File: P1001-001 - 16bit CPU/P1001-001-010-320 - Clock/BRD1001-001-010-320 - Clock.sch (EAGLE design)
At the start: 15 parts, among them IC1 74HC192D, IC12 74AC245DW, IC2 74HC192D, IC27 MEGA8535-A, IC3 74HC192D, IC4 74HC192D, IC7 74AC245DW, J1 22-27-2041-04

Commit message: Finish ALI Counter
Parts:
- removed BOTTOMBUS, FRONTBUS: (no value), con-harting-ml:ML16
- removed IC1, IC2: 74HC192D, 74xx-eu:74HC192D
- removed IC12, IC7: 74AC245DW, 74xx-eu:74AC245DW
- removed IC27: MEGA8535-A, atmel:MEGA8535-A
- removed J1: 22-27-2041-04, con-molex:22-27-2041-04
- removed JP2: (no value), jumper:JP4E
- removed RN2: (no value), resistor-dil:10R-NSOMC
- removed SV5: (no value), con-harting-ml:ML6
- added !CLOCKPIN, VCC_GND1, VCC_GND2: (no value), con-harting-ml:ML16
- added C1, C5, C6: .01uF, rcl:C-USC1206
- added C2: 1uF, rcl:C-USC1206
- added C7: .1uF, rcl:C-USC1206
- added CN1: (no value), adafruit:DCBARRELPTH
- added IC5: 74LS32D, 74xx-us:74LS32D
- added JP1: (no value), jumper:JP2E
- added LED1: (no value), led:LED5MM
- added R1, R2, R4, R5, R7: 1k, rcl:R-US_M1206
- added R3: 1M, rcl:R-US_M1206
- added R6: (no value), rcl:R-US_M1206
- added S1: (no value), switch-omron:40-XX
- added U$10, U$11, U$12, U$5, U$6, U$7, U$8, U$9: AZ1117E, 16bit:AZ1117E
- added U$2, U$3, U$4: NA555, 16bit:NA555
- IC3: value 74HC192D -> 74ALS04D; device 74xx-eu:74HC192D -> 74xx-us:74ALS04D
- IC4: value 74HC192D -> 74ALS08D; device 74xx-eu:74HC192D -> 74xx-us:74ALS08D
- U$1: value 4-DIGIT-7-SEGMENT -> 3310H-001-105L; device ADAFRUIT:4-DIGIT-7-SEGMENT -> 16bit:3310H-001-105L
- renumbered BACKBUS to CLOCKPIN
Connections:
- removed net !DEC: IC1A.DN, JP2.3
- removed net !INC: IC1A.UP, JP2.2
- removed net !REG_IN: IC1A.LD, IC2A.LD, IC3A.LD, IC4A.LD, JP2.1
- removed net !REG_OUT: IC12A.G, IC7A.G, JP2.4
- removed net A: IC27.(ADC0)PA0, RN2A.2
- removed net B: IC27.(ADC1)PA1, RN2B.2
- removed net BUS0: CLOCKPIN.1, FRONTBUS.1, IC12A.A8, IC1A.D
- removed net BUS1: CLOCKPIN.2, FRONTBUS.2, IC12A.A7, IC1A.C
- removed net BUS10: CLOCKPIN.11, FRONTBUS.11, IC3A.B, IC7A.A6
- removed net BUS11: CLOCKPIN.12, FRONTBUS.12, IC3A.A, IC7A.A5
- removed net BUS12: CLOCKPIN.13, FRONTBUS.13, IC4A.D, IC7A.A4
- removed net BUS13: CLOCKPIN.14, FRONTBUS.14, IC4A.C, IC7A.A3
- removed net BUS14: CLOCKPIN.15, FRONTBUS.15, IC4A.B, IC7A.A2
- removed net BUS15: CLOCKPIN.16, FRONTBUS.16, IC4A.A, IC7A.A1
- removed net BUS2: CLOCKPIN.3, FRONTBUS.3, IC12A.A6, IC1A.B
- removed net BUS3: CLOCKPIN.4, FRONTBUS.4, IC12A.A5, IC1A.A
- removed net BUS4: CLOCKPIN.5, FRONTBUS.5, IC12A.A4, IC2A.D
- removed net BUS5: CLOCKPIN.6, FRONTBUS.6, IC12A.A3, IC2A.C
- removed net BUS6: CLOCKPIN.7, FRONTBUS.7, IC12A.A2, IC2A.B
- removed net BUS7: CLOCKPIN.8, FRONTBUS.8, IC12A.A1, IC2A.A
- removed net BUS8: CLOCKPIN.9, FRONTBUS.9, IC3A.D, IC7A.A8
- removed net BUS9: CLOCKPIN.10, FRONTBUS.10, IC3A.C, IC7A.A7
- removed net C: IC27.(ADC2)PA2, RN2C.2
- removed net CLEAR: IC1A.CLR, IC2A.CLR, IC3A.CLR, IC4A.CLR, J1-4.S
- removed net D: IC27.(ADC3)PA3, RN2D.2
- removed net DIG0: IC27.(T0/XCK)PB0, U$1.DIG1
- removed net DIG1: IC27.(T1)PB1, U$1.DIG2
- removed net DIG2: IC27.(AIN0/INT2)PB2, U$1.DIG3
- removed net DIG3: IC27.(AIN1/OC0)PB3, U$1.DIG4
- removed net DP: IC27.(ADC7)PA7, RN2H.2
- removed net E: IC27.(ADC4)PA4, RN2E.2
- removed net F: IC27.(ADC5)PA5, RN2F.2
- removed net G: IC27.(ADC6)PA6, RN2G.2
- removed net N$18: IC27.(MOSI)PB5, SV5.3
- removed net N$19: IC27.(SCK)PB7, SV5.4
- removed net N$20: IC27.(MISO)PB6, SV5.6
- removed net N$21: IC27.RESET, SV5.2
- removed net N$24: RN2A.1, U$1.A
- removed net N$25: RN2B.1, U$1.B
- removed net N$26: RN2C.1, U$1.C
- removed net N$27: RN2D.1, U$1.D
- removed net N$28: RN2E.1, U$1.E
- removed net N$29: RN2F.1, U$1.F
- removed net N$30: RN2G.1, U$1.G
- removed net N$31: RN2H.1, U$1.DP
- removed net N$7: IC3A.BO, IC4A.DN
- removed net SIGNAL0: BOTTOMBUS.1, IC12A.B8, IC1A.QD, IC27.(RXD)PD0
- removed net SIGNAL1: BOTTOMBUS.2, IC12A.B7, IC1A.QC, IC27.(TXD)PD1
- removed net SIGNAL10: BOTTOMBUS.11, IC27.PC2, IC3A.QB, IC7A.B6
- removed net SIGNAL11: BOTTOMBUS.12, IC27.PC3, IC3A.QA, IC7A.B5
- removed net SIGNAL12: BOTTOMBUS.13, IC27.PC4, IC4A.QD, IC7A.B4
- removed net SIGNAL13: BOTTOMBUS.14, IC27.PC5, IC4A.QC, IC7A.B3
- removed net SIGNAL14: BOTTOMBUS.15, IC27.(TOSC1)PC6, IC4A.QB, IC7A.B2
- removed net SIGNAL15: BOTTOMBUS.16, IC27.(TOSC2)PC7, IC4A.QA, IC7A.B1
- removed net SIGNAL2: BOTTOMBUS.3, IC12A.B6, IC1A.QB, IC27.(INT0)PD2
- removed net SIGNAL3: BOTTOMBUS.4, IC12A.B5, IC1A.QA, IC27.(INT1)PD3
- removed net SIGNAL4: BOTTOMBUS.5, IC12A.B4, IC27.(OC1B)PD4, IC2A.QD
- removed net SIGNAL5: BOTTOMBUS.6, IC12A.B3, IC27.(OC1A)PD5, IC2A.QC
- removed net SIGNAL6: BOTTOMBUS.7, IC12A.B2, IC27.(ICP)PD6, IC2A.QB
- removed net SIGNAL7: BOTTOMBUS.8, IC12A.B1, IC27.(OC2)PD7, IC2A.QA
- removed net SIGNAL8: BOTTOMBUS.9, IC27.PC0(SCL), IC3A.QD, IC7A.B8
- removed net SIGNAL9: BOTTOMBUS.10, IC27.PC1(SDA), IC3A.QC, IC7A.B7
- new net !CLK: !CLOCKPIN.1, !CLOCKPIN.10, !CLOCKPIN.11, !CLOCKPIN.12, !CLOCKPIN.13, !CLOCKPIN.14, !CLOCKPIN.15, !CLOCKPIN.16, !CLOCKPIN.2, !CLOCKPIN.3, !CLOCKPIN.4, !CLOCKPIN.5, !CLOCKPIN.6, !CLOCKPIN.7, !CLOCKPIN.8, !CLOCKPIN.9, IC3C.O
- new net !HALT: IC4C.I1
- new net IN: CN1.PWR, U$10.INPUT, U$11.INPUT, U$12.INPUT, U$5.INPUT, U$6.INPUT, U$7.INPUT, U$8.INPUT, U$9.INPUT
- new net N$10: C6.1, U$4.CONT
- new net N$11: C5.1, U$3.CONT
- new net N$12: IC3A.I, IC4A.I0, U$4.OUT
- new net N$13: IC4A.I1, JP1.3, R1.1, R2.1, U$2.OUT
- new net N$14: IC4B.I0, U$3.OUT
- new net N$15: IC3A.O, IC4B.I1
- new net N$16: IC4A.O, IC5A.I0
- new net N$17: IC4B.O, IC5A.I1
- new net N$22: IC4C.I0, IC5A.O
- new net N$8: C2.1, U$1.START1, U$2.THRES, U$2.TRIG
- new net N$9: C1.1, U$2.CONT
- new net VCC1: S1.S, S1.S1, U$3.TRIG
- net CLK: now also CLOCKPIN.1, CLOCKPIN.10, CLOCKPIN.11, CLOCKPIN.12, CLOCKPIN.13, CLOCKPIN.14, CLOCKPIN.15, CLOCKPIN.16, CLOCKPIN.2, CLOCKPIN.3, CLOCKPIN.4, CLOCKPIN.5, CLOCKPIN.6, CLOCKPIN.7, CLOCKPIN.8, CLOCKPIN.9, IC3C.I, IC4C.O, LED1.A; no longer J1-3.S
- net GND: now also C1.2, C2.2, C5.2, C6.2, C7.2, CN1.GND, JP1.2, R6.1, U$10.GND, U$11.GND, U$12.GND, U$2.GND, U$3.GND, U$4.GND, U$4.THRES, U$5.GND, U$6.GND, U$7.GND, U$8.GND, U$9.GND, VCC_GND1.1, VCC_GND1.11, VCC_GND1.13, VCC_GND1.15, VCC_GND1.3, VCC_GND1.5, VCC_GND1.7, VCC_GND1.9, VCC_GND2.1, VCC_GND2.11, VCC_GND2.13, VCC_GND2.15, VCC_GND2.3, VCC_GND2.5, VCC_GND2.7, VCC_GND2.9; no longer IC12A.DIR, IC27.AREF, IC27.GND, IC27.GND1, IC27.GND2, IC27.GND@1, IC7A.DIR, J1-1.S, SV5.1
- net N$1: now also R5.1, R7.1, U$2.DISCH; no longer IC4A.BO
- net N$2: now also R7.2, U$1.SCRUB1; no longer IC1A.CO, IC2A.UP
- net N$3: now also LED1.C, R6.2; no longer IC1A.BO, IC2A.DN
- net N$4: now also R2.2, U$4.TRIG; no longer IC2A.CO, IC3A.UP
- net N$5: now also R4.2, S1.P, S1.P1; no longer IC2A.BO, IC3A.DN
- net N$6: now also C7.1, R3.1, U$3.DISCH, U$3.THRES; no longer IC3A.CO, IC4A.UP
- net VCC: now also JP1.1, R1.2, R3.2, R4.1, R5.2, U$10.OUTPUT, U$11.OUTPUT, U$12.OUTPUT, U$2.RESET, U$2.VCC, U$3.RESET, U$3.VCC, U$4.RESET, U$4.VCC, U$5.OUTPUT, U$6.OUTPUT, U$7.OUTPUT, U$8.OUTPUT, U$9.OUTPUT, VCC_GND1.10, VCC_GND1.12, VCC_GND1.14, VCC_GND1.16, VCC_GND1.2, VCC_GND1.4, VCC_GND1.6, VCC_GND1.8, VCC_GND2.10, VCC_GND2.12, VCC_GND2.14, VCC_GND2.16, VCC_GND2.2, VCC_GND2.4, VCC_GND2.6, VCC_GND2.8; no longer IC27.AVCC, IC27.VCC, IC27.VCC1, IC27.VCC2, J1-2.S, SV5.5

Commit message: Check in the first try at soldering up the board
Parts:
- added AUTO, PULSE, SWITCH: NA555, 16bit:NA555
- added JP2: (no value), jumper:JP2E
- added U$13: AZ1117E, 16bit:AZ1117E
- U$2, U$3, U$4: value NA555 -> AZ1117E; device 16bit:NA555 -> 16bit:AZ1117E
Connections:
- removed net N$12: IC3A.I, IC4A.I0, U$4.OUT
- removed net N$5 (its old number): R4.2, S1.P, S1.P1
- removed net VCC1: S1.S, S1.S1, U$3.TRIG
- new net AUTOOUT: AUTO.OUT, IC4A.I0
- new net N$7: PULSE.TRIG, R4.1, S1.S, S1.S1
- new net PULSEOUT: IC4B.I0, PULSE.OUT
- new net SWITCHOUT: IC3A.I, IC4A.I1, SWITCH.OUT
- net !HALT: now also JP2.3
- net GND: now also AUTO.GND, PULSE.GND, S1.P, S1.P1, SWITCH.GND, SWITCH.THRES, U$13.GND; no longer C1.2, U$4.THRES
- net IN: now also U$13.INPUT, U$2.INPUT, U$3.INPUT, U$4.INPUT
- net N$1: now also AUTO.THRES, AUTO.TRIG, C2.1, U$1.START1; no longer R5.1, R7.1, U$2.DISCH
- net N$10: now also PULSE.DISCH, R3.1; no longer C6.1, U$4.CONT
- net N$11: now also C6.1, SWITCH.CONT; no longer C5.1, U$3.CONT
- net N$13: now also SWITCH.RESET; no longer IC4A.I1, R1.1, U$2.OUT
- net N$14: now also JP1.1, R1.1, SWITCH.TRIG; no longer IC4B.I0, U$3.OUT
- net N$4: now also AUTO.CONT, C1.1; no longer R2.2, U$4.TRIG
- net N$6: now also AUTO.DISCH, R5.1, R7.1; no longer C7.1, R3.1, U$3.DISCH, U$3.THRES
- net N$8: now also C7.1, PULSE.THRES; no longer C2.1, U$1.START1, U$2.THRES, U$2.TRIG
- net N$9: now also C5.1, PULSE.CONT; no longer C1.1, U$2.CONT
- net VCC: now also AUTO.RESET, AUTO.VCC, C1.2, PULSE.RESET, PULSE.VCC, R2.2, R4.2, SWITCH.VCC, U$13.OUTPUT, U$2.OUTPUT, U$3.OUTPUT, U$4.OUTPUT; no longer JP1.1, R4.1, U$2.RESET, U$2.VCC, U$3.RESET, U$3.VCC, U$4.RESET, U$4.VCC
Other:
- moved on the sheet: C1, C2, C5, C6, C7, JP1, R1, R2, R3, R4, R5, R7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

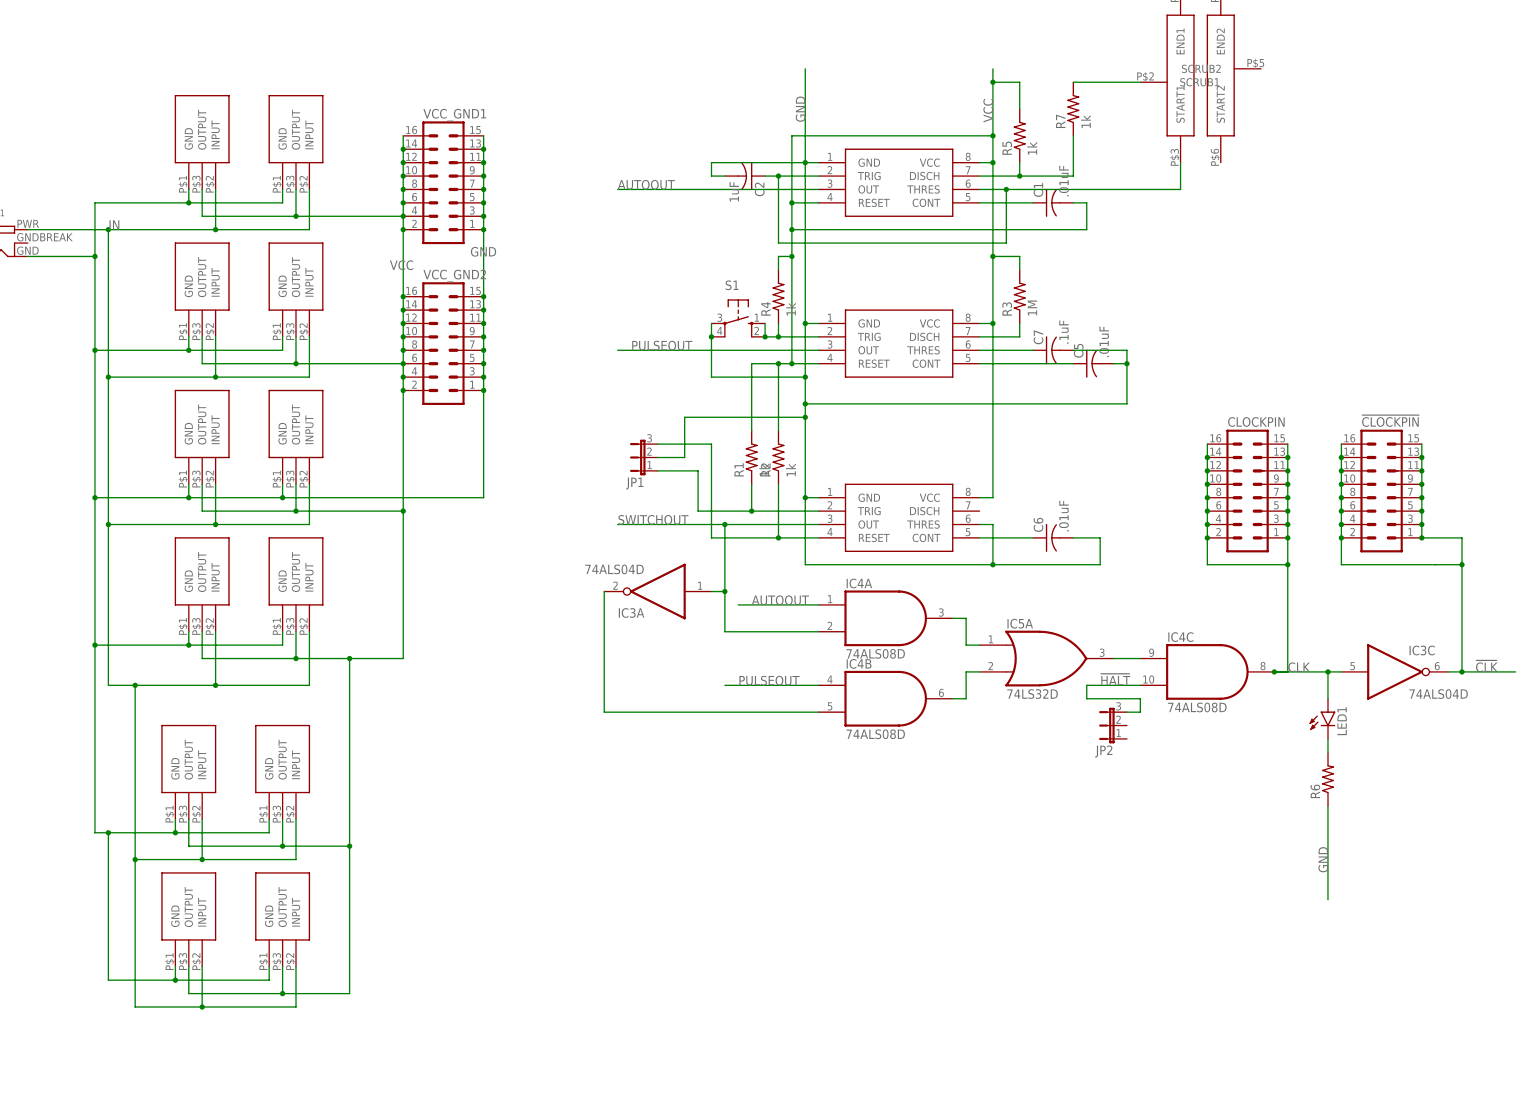
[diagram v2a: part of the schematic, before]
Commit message: add ram to Memory
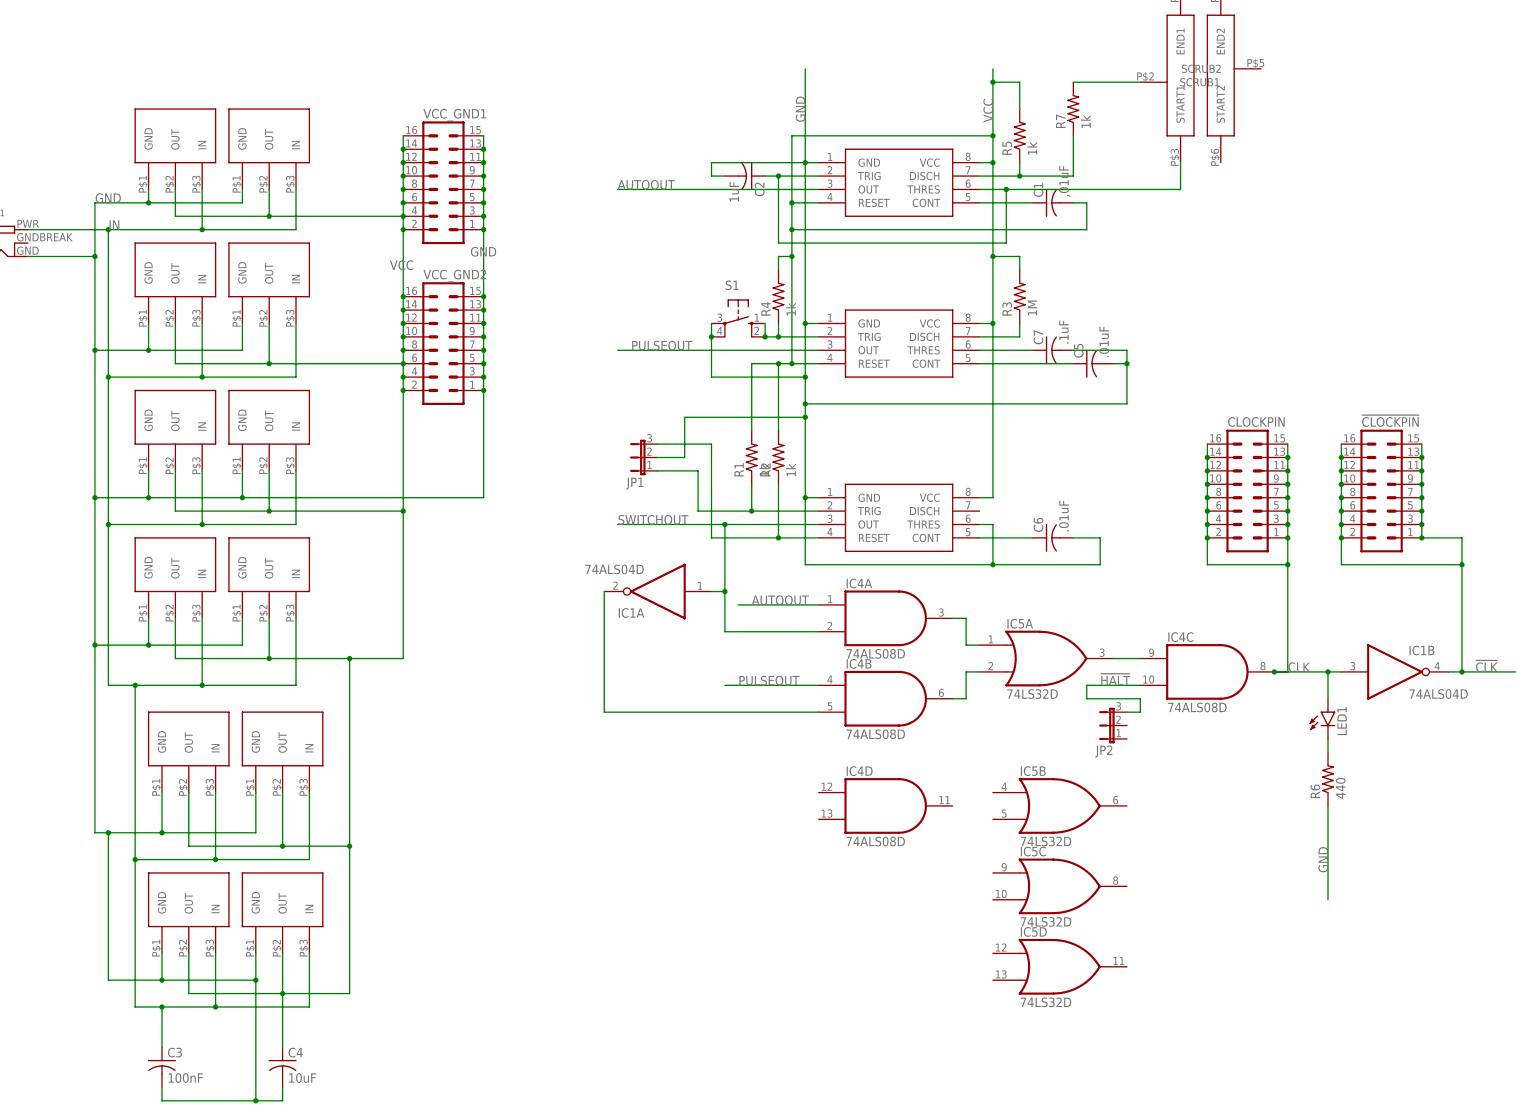
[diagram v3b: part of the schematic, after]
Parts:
- added C3: 100nF, rcl:C-US025-024X044
- added C4: 10uF, rcl:C-US025-024X044
- C1: value .01uF -> ,01uF; device rcl:C-USC1206 -> rcl:C-US025-024X044
- C2, C5, C6, C7: device rcl:C-USC1206 -> rcl:C-US025-024X044
- R1, R2, R3, R4, R5, R7: device rcl:R-US_M1206 -> rcl:R-US_0204/2V
- R6: value (none) -> 440; device rcl:R-US_M1206 -> rcl:R-US_0204/2V
- U$10, U$11, U$12, U$13, U$2, U$3, U$4, U$5, U$6, U$7, U$8, U$9: value AZ1117E -> LD1117S33TR; device 16bit:AZ1117E -> P1001-001-310 - Eagle Library:LD1117S33TR
- renumbered IC3 to IC1
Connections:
- net !CLK: now also IC1B.O; no longer IC1C.O
- net CLK: now also IC1B.I; no longer IC1C.I
- net GND: now also C3.2, C4.2
- net IN: now also C3.1, U$10.IN, U$11.IN, U$12.IN, U$13.IN, U$2.IN, U$3.IN, U$4.IN, U$5.IN, U$6.IN, U$7.IN, U$8.IN, U$9.IN; no longer U$10.INPUT, U$11.INPUT, U$12.INPUT, U$13.INPUT, U$2.INPUT, U$3.INPUT, U$4.INPUT, U$5.INPUT, U$6.INPUT, U$7.INPUT, U$8.INPUT, U$9.INPUT
- net VCC: now also C4.1, U$10.OUT, U$11.OUT, U$12.OUT, U$13.OUT, U$2.OUT, U$3.OUT, U$4.OUT, U$5.OUT, U$6.OUT, U$7.OUT, U$8.OUT, U$9.OUT; no longer U$10.OUTPUT, U$11.OUTPUT, U$12.OUTPUT, U$13.OUTPUT, U$2.OUTPUT, U$3.OUTPUT, U$4.OUTPUT, U$5.OUTPUT, U$6.OUTPUT, U$7.OUTPUT, U$8.OUTPUT, U$9.OUTPUT
